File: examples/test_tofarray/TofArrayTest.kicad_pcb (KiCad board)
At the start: 2 copper layers, 30 x 55 mm, 44 parts, among them sw1 3.9x2.9mm Switch

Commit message: updated netlist
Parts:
- removed leds.led[5].package, leds.led[6].package, leds.led[7].package: KT-0603R (Hubei KENTO Elec) - Red 615~630nm 1.9~2.2V 0603 L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, LED_SMD:LED_0603_1608Metric
- removed leds.led[5].res, leds.led[6].res, leds.led[7].res: 0603WAF1001T5E (UNI-ROYAL(Uniroyal Elec)) - ±1% 1/10W Thick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, Resistor_SMD:R_0603_1608Metric
- removed the mcu.crystal.package at (128.1, -34.3)
- removed the mcu.swd at (88.0, -19.0)
- added i2c_pull.scl_res: 0603WAF4701T5E (UNI-ROYAL(Uniroyal Elec)) - ±1% 1/10W Thick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, Resistor_SMD:R_0603_1608Metric, F.Cu at (135.2, 48.9)
- added i2c_pull.sda_res: 0603WAF4701T5E (UNI-ROYAL(Uniroyal Elec)) - ±1% 1/10W Thick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, Resistor_SMD:R_0603_1608Metric, F.Cu at (131.2, 48.9)
- added mcu.crystal.package: X322512MSB4SI (Yangxing Tech) - 12MHz SMD Crystal Resonator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, Crystal_SMD_3225-4Pin_3.2x2.5mm, F.Cu at (211.1, 40.7)
- added mcu.swd: SWD, Connector:Tag-Connect_TC2050-IDC-FP_2x05_P1.27mm_Vertical, F.Cu at (170.0, 53.0)
- added rgb.blue_res: 0603WAF1001T5E (UNI-ROYAL(Uniroyal Elec)) - ±1% 1/10W Thick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, Resistor_SMD:R_0603_1608Metric, F.Cu at (132.1, 41.3)
- added rgb.green_res: 0603WAF1001T5E (UNI-ROYAL(Uniroyal Elec)) - ±1% 1/10W Thick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, Resistor_SMD:R_0603_1608Metric, F.Cu at (136.1, 38.8)
- added rgb.package: EAST1616RGBB2 (Everlight Electronics Co Ltd), LED_SMD:LED_LiteOn_LTST-C19HE1WT, F.Cu at (135.7, 41.9)
- added rgb.red_res: 0603WAF1001T5E (UNI-ROYAL(Uniroyal Elec)) - ±1% 1/10W Thick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, Resistor_SMD:R_0603_1608Metric, F.Cu at (132.1, 38.8)
- added spk: B2B-PH-K (JST), Connector_JST:JST_PH_B2B-PH-K_1x02_P2.00mm_Vertical, F.Cu at (117.5, 50.3)
- added spk_dac.c: CL10B473KB8NNNC (Samsung Electro-Mechanics) - 50V 47nF X7R 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, Capacitor_SMD:C_0603_1608Metric, F.Cu at (116.5, 58.4)
- added spk_dac.r: 0603WAF1001T5E (UNI-ROYAL(Uniroyal Elec)) - ±1% 1/10W Thick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, Resistor_SMD:R_0603_1608Metric, F.Cu at (120.5, 58.4)
- added spk_drv.bulk_cap: CL21A475KAQNNNE (Samsung Electro-Mechanics) - 25V 4.7uF X5R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, Capacitor_SMD:C_0805_2012Metric, F.Cu at (164.9, 46.9)
- added spk_drv.ic: TPA2005D1 (Texas Instruments), Package_SO:MSOP-8-1EP_3x3mm_P0.65mm_EP1.68x1.88mm_ThermalVias, F.Cu at (236.9, 50.3)
- added spk_drv.inn_cap: CL10A105KB8NNNC (Samsung Electro-Mechanics) - 50V 1uF X5R ±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, Capacitor_SMD:C_0603_1608Metric, F.Cu at (124.5, 38.8)
- added spk_drv.inn_res: 0603WAF3002T5E (UNI-ROYAL(Uniroyal Elec)) - ±1% 1/10W Thick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, Resistor_SMD:R_0603_1608Metric, F.Cu at (116.5, 38.8)
- added spk_drv.inp_cap: CL10A105KB8NNNC (Samsung Electro-Mechanics) - 50V 1uF X5R ±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, Capacitor_SMD:C_0603_1608Metric, F.Cu at (116.5, 41.3)
- added spk_drv.inp_res: 0603WAF3002T5E (UNI-ROYAL(Uniroyal Elec)) - ±1% 1/10W Thick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, Resistor_SMD:R_0603_1608Metric, F.Cu at (120.5, 38.8)
- added spk_drv.pwr_cap: CC0603KRX7R9BB104 (YAGEO) - 50V 100nF X7R ±10% 0603 Multila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, Capacitor_SMD:C_0603_1608Metric, F.Cu at (120.5, 41.3)
- added tof.elt[0].ic: VL53L0X (STMicroelectronics), OptoDevice:ST_VL53L0X, F.Cu at (155.5, 54.3)
- added tof.elt[0].vdd_cap[0]: CC0603KRX7R9BB104 (YAGEO) - 50V 100nF X7R ±10% 0603 Multila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, Capacitor_SMD:C_0603_1608Metric, F.Cu at (162.7, 38.8)
- added tof.elt[0].vdd_cap[1]: CL21A475KAQNNNE (Samsung Electro-Mechanics) - 25V 4.7uF X5R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, Capacitor_SMD:C_0805_2012Metric, F.Cu at (158.5, 39.0)
- added tof.elt[1].ic: VL53L0X (STMicroelectronics), OptoDevice:ST_VL53L0X, F.Cu at (170.8, 39.5)
- added tof.elt[1].vdd_cap[0]: CC0603KRX7R9BB104 (YAGEO) - 50V 100nF X7R ±10% 0603 Multila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, Capacitor_SMD:C_0603_1608Metric, F.Cu at (147.4, 48.2)
- added tof.elt[1].vdd_cap[1]: CL21A475KAQNNNE (Samsung Electro-Mechanics) - 25V 4.7uF X5R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, Capacitor_SMD:C_0805_2012Metric, F.Cu at (143.1, 48.5)
- added tof.elt[2].ic: VL53L0X (STMicroelectronics), OptoDevice:ST_VL53L0X, F.Cu at (240.0, 44.0)
- added tof.elt[2].vdd_cap[0]: CC0603KRX7R9BB104 (YAGEO) - 50V 100nF X7R ±10% 0603 Multila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, Capacitor_SMD:C_0603_1608Metric, F.Cu at (132.7, 58.4)
- added tof.elt[2].vdd_cap[1]: CL21A475KAQNNNE (Samsung Electro-Mechanics) - 25V 4.7uF X5R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, Capacitor_SMD:C_0805_2012Metric, F.Cu at (128.5, 58.7)
- added tof.elt[3].ic: VL53L0X (STMicroelectronics), OptoDevice:ST_VL53L0X, F.Cu at (155.5, 47.3)
- added tof.elt[3].vdd_cap[0]: CC0603KRX7R9BB104 (YAGEO) - 50V 100nF X7R ±10% 0603 Multila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, Capacitor_SMD:C_0603_1608Metric, F.Cu at (228.0, 49.4)
- added tof.elt[3].vdd_cap[1]: CL21A475KAQNNNE (Samsung Electro-Mechanics) - 25V 4.7uF X5R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, Capacitor_SMD:C_0805_2012Metric, F.Cu at (223.7, 49.6)
- added tof.elt[4].ic: VL53L0X (STMicroelectronics), OptoDevice:ST_VL53L0X, F.Cu at (140.9, 57.5)
- added tof.elt[4].vdd_cap[0]: CC0603KRX7R9BB104 (YAGEO) - 50V 100nF X7R ±10% 0603 Multila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, Capacitor_SMD:C_0603_1608Metric, F.Cu at (151.1, 38.8)
- added tof.elt[4].vdd_cap[1]: CL21A475KAQNNNE (Samsung Electro-Mechanics) - 25V 4.7uF X5R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, Capacitor_SMD:C_0805_2012Metric, F.Cu at (146.9, 39.0)
- mcu.crystal.cap_a, mcu.crystal.cap_b: value CL10C100JB8NNNC (Samsung Electro-Mechanics) - 50V 10pF C0G ±5% 0603 Multilayer Ceramic Capacitors MLCC - SMD/SMT ROHS -> CL10C330JB8NNNC (Samsung Electro-Mechanics) - 50V 33pF C0G ±5% 0603 Multilayer Ceramic Capacitors MLCC - SMD/SMT ROHS
- moved jlc_th3 135.0 mm to (248.0, 58.0)
- moved leds.led[0].res 117.0 mm to (237.0, 57.0)
- moved leds.led[1].package 111.9 mm to (199.3, 54.1)
- moved leds.led[2].package 111.9 mm to (210.7, 47.5)
- moved leds.led[2].res 111.9 mm to (229.8, 39.8)
- moved leds.led[3].res 111.9 mm to (214.8, 53.2)
- moved leds.led[4].package 111.9 mm to (222.1, 39.8)
- moved mcu.crystal.cap_a 111.9 mm to (187.5, 54.1)
- moved mcu.crystal.cap_b 111.9 mm to (191.5, 54.1)
- moved mcu.pwr_cap[0] 111.9 mm to (197.4, 40.0)
- moved mcu.pwr_cap[2] 111.9 mm to (197.2, 45.3)
- moved mcu.usb_pull 111.9 mm to (187.5, 48.2)
- moved mcu.vdda_cap_0 111.9 mm to (191.5, 48.2)
- moved mcu.vdda_cap_1 111.9 mm to (197.2, 42.8)
- moved mcu.pwr_cap[1] 111.9 mm to (201.2, 42.8)
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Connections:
- net leds.led[1].package.k renamed leds.led[1].res.a
- net leds.led[2].package.k renamed leds.led[2].res.a
- net leds.led[4].package.k renamed leds.led[4].res.a
- net mcu.gpio.leds_1 renamed leds_chain_0.1
- net usb.usb.dm renamed usb_chain_0.d_N
- net usb.usb.dp renamed usb_chain_0.d_P
- leds.led[0].package pad 2: mcu.gpio.leds_0 -> leds_chain_0.0
- leds.led[2].package pad 2: mcu.gpio.leds_2 -> leds_chain_0.2
- leds.led[3].package pad 2: mcu.gpio.leds_3 -> leds_chain_0.3
- leds.led[4].package pad 2: leds.signals.4 -> leds_chain_0.4
- mcu.ic pad 10: mcu.gpio.sw1 -> spk_chain_0
- mcu.ic pad 11: leds.signals.4 -> sw1_chain_0
- mcu.ic pad 12: leds.signals.5 -> tof.xshut.4
- mcu.ic pad 13: mcu.gpio.leds_0 -> mcu.gpio.tof_xshut_1
- mcu.ic pad 14: mcu.gpio.leds_2 -> tof.xshut.0
- mcu.ic pad 15: mcu.gpio.leds_7 -> mcu.gpio.tof_xshut_2
- mcu.ic pad 16: mcu.gpio.leds_3 -> tof.xshut.3
- mcu.ic pad 17: leds.signals.6 -> leds_chain_0.4
- mcu.ic pad 19: (no net) -> leds_chain_0.0
- mcu.ic pad 20: (no net) -> leds_chain_0.2
- mcu.ic pad 21: (no net) -> i2c_chain_0.scl
- mcu.ic pad 22: (no net) -> i2c_chain_0.sda
- mcu.ic pad 25: (no net) -> leds_chain_0.3
- mcu.ic pad 26: (no net) -> rgb_chain_0.red
- mcu.ic pad 27: (no net) -> rgb_chain_0.green
- mcu.ic pad 28: (no net) -> rgb_chain_0.blue
- mcu.ic pad 34: mcu.swd.swd.swdio -> mcu.ic.swd.swdio
- mcu.ic pad 39: mcu.swd.swd.swo -> mcu.ic.swd.swo
- mcu.ic pad 7: mcu.swd.swd.reset -> mcu.ic.swd.reset
- sw1 pad 2: mcu.gpio.sw1 -> sw1_chain_0
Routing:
- net gnd: track 56.3 -> 54.3 mm, vias 5 -> 2
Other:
- board size 30 x 55 mm -> 200 x 25 mm

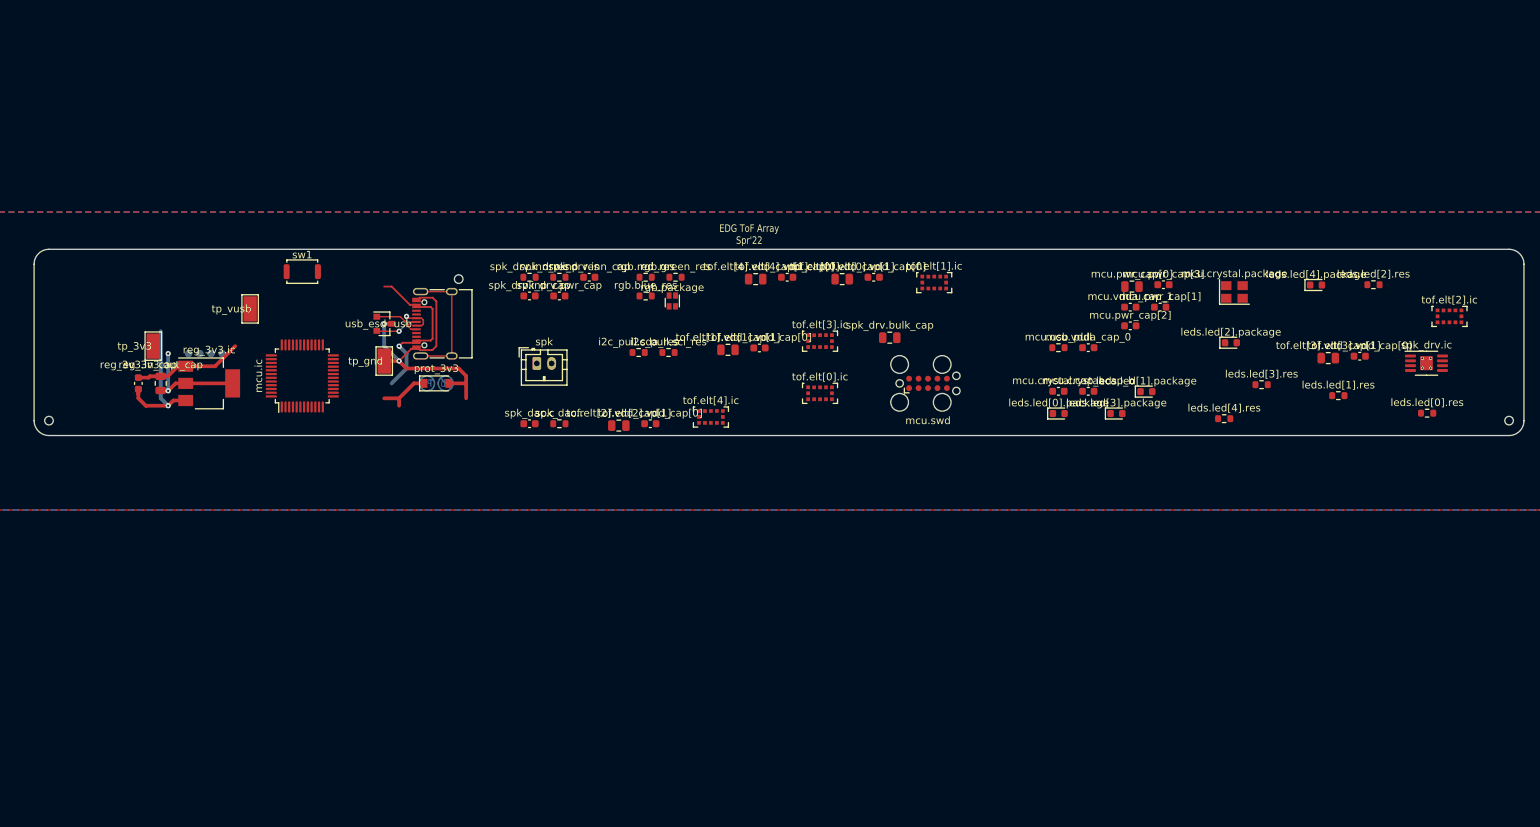
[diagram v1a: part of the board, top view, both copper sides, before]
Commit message: coarse placement of ToF array
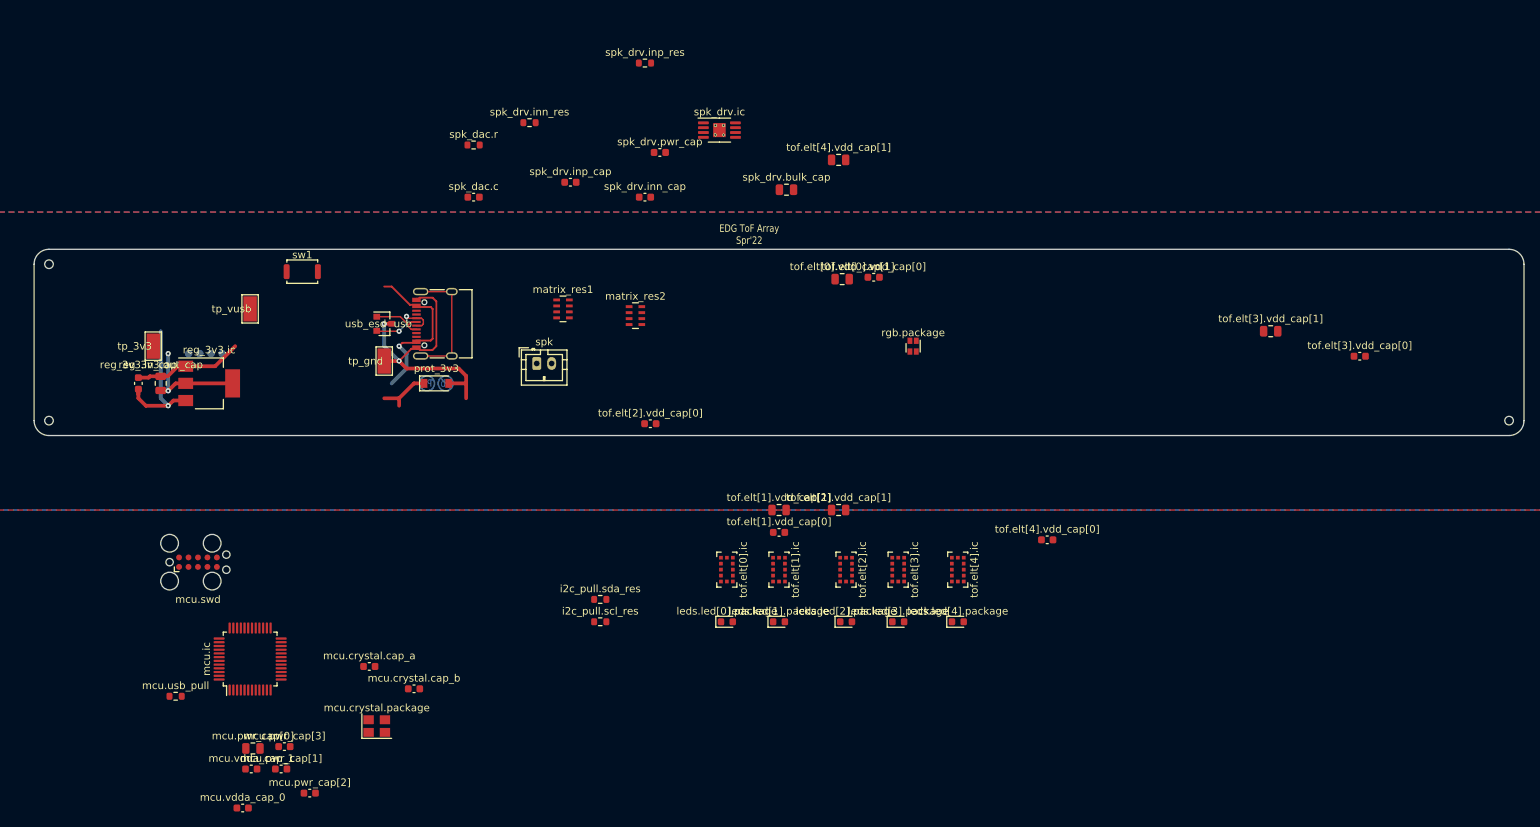
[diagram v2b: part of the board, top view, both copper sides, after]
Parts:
- removed leds.led[0].res, leds.led[1].res, leds.led[2].res, leds.led[3].res, leds.led[4].res, rgb.blue_res, rgb.green_res, rgb.red_res: 0603WAF1001T5E (UNI-ROYAL(Uniroyal Elec)) - ±1% 1/10W Thick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, Resistor_SMD:R_0603_1608Metric
- added matrix_res1: 4D03WGJ0102T5E (UNI-ROYAL(Uniroyal Elec)) - 4 ±5% 8 1kΩ 1/1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, Resistor_SMD:R_Array_Concave_4x0603, F.Cu at (121.0, 43.0)
- added matrix_res2: 4D03WGJ0102T5E (UNI-ROYAL(Uniroyal Elec)) - 4 ±5% 8 1kΩ 1/1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, Resistor_SMD:R_Array_Concave_4x0603, F.Cu at (130.7, 43.9)
- moved mcu.pwr_cap[0] 133.3 mm to (79.4, 102.0)
- moved mcu.vdda_cap_1 133.3 mm to (79.2, 104.8)
- moved mcu.pwr_cap[1] 133.3 mm to (83.2, 104.8)
- moved mcu.pwr_cap[3] 133.3 mm to (83.6, 101.8)
- moved mcu.vdda_cap_0 129.2 mm to (78.0, 110.0)
- moved mcu.crystal.package 129.0 mm to (96.0, 99.0)
- moved mcu.usb_pull 127.4 mm to (69.0, 95.0)
- moved mcu.pwr_cap[2] 126.8 mm to (87.0, 108.0)
- moved mcu.swd 100.9 mm to (72.0, 77.0)
- moved spk_drv.ic 99.9 mm to (142.0, 19.0)
- moved mcu.crystal.cap_a 99.6 mm to (95.0, 91.0)
- moved mcu.crystal.cap_b 98.9 mm to (101.0, 94.0)
- moved tof.elt[2].ic 87.8 mm to (159.0, 78.0), turned to 270 degrees
- moved leds.led[4].package 66.0 mm to (174.0, 85.0)
- moved leds.led[2].package 63.8 mm to (159.0, 85.0)
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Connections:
- net mcu.crystal.crystal.b renamed mcu.ic.osc.xtal_out
- net mcu.gpio.tof_xshut_1 renamed tof.xshut.1
- net mcu.gpio.tof_xshut_2 renamed tof.xshut.2
- net mcu.ic.swd.reset renamed mcu.swd.swd.reset
- net mcu.ic.swd.swclk renamed mcu.swd.swd.swclk
- net tof.xshut.0 renamed mcu.gpio.tof_xshut_0
- net tof.xshut.4 renamed mcu.gpio.tof_xshut_4
- net usb.shield renamed usb.S1
- leds.led[0].package pad 1: leds.led[0].res.a -> matrix_res1.a.0
- leds.led[1].package pad 1: leds.led[1].res.a -> matrix_res1.a.1
- leds.led[2].package pad 1: leds.led[2].res.a -> matrix_res1.a.2
- leds.led[3].package pad 1: leds.led[3].package.k -> matrix_res1.a.3
- leds.led[4].package pad 1: leds.led[4].res.a -> matrix_res2.a.0
- mcu.ic pad 26: rgb_chain_0.red -> rgb_chain_0.green
- mcu.ic pad 27: rgb_chain_0.green -> rgb_chain_0.blue
- mcu.ic pad 28: rgb_chain_0.blue -> rgb_chain_0.red
- rgb.package pad 1: rgb.package.k_blue -> matrix_res2.a.3
- rgb.package pad 3: rgb.red_res.a -> matrix_res2.a.1
- rgb.package pad 4: rgb.package.k_green -> matrix_res2.a.2

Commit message: continued coarse placement
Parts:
- moved tof.elt[3].vdd_cap[0] 66.3 mm to (166.0, 73.0)
- moved tof.elt[3].vdd_cap[1] 55.5 mm to (166.0, 70.0)
- moved tof.elt[4].vdd_cap[1] 49.6 mm to (174.0, 70.0)
- moved tof.elt[0].vdd_cap[0] 39.5 mm to (143.0, 73.0)
- moved tof.elt[0].vdd_cap[1] 34.6 mm to (143.0, 70.0)
- moved mcu.crystal.package 30.5 mm to (68.0, 87.0), turned to 90 degrees
- moved mcu.crystal.cap_b 30.1 mm to (72.0, 86.0)
- moved tof.elt[2].vdd_cap[0] 30.1 mm to (159.0, 73.0)
- moved spk_drv.bulk_cap 24.2 mm to (129.0, 17.0)
- moved mcu.crystal.cap_a 23.2 mm to (72.0, 88.0)
- moved mcu.pwr_cap[3] 21.1 mm to (80.0, 81.0), turned to 180 degrees
- moved mcu.swd 20.1 mm to (52.0, 75.0)
- moved mcu.vdda_cap_0 18.4 mm to (71.0, 93.0), turned to 90 degrees
- moved mcu.pwr_cap[2] 18.1 mm to (89.0, 90.0), turned to 270 degrees
- moved mcu.pwr_cap[0] 16.7 mm to (91.0, 90.0), turned to 270 degrees
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
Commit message: coarse placement 2
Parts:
- moved matrix_res1 81.9 mm to (193.0, 4.00)
- moved matrix_res2 81.9 mm to (202.7, 4.91)
- moved tp_gnd 81.9 mm to (169.0, 11.0)
- moved leds.led[0].package 78.2 mm to (70.0, 57.0)
- moved tof.elt[0].ic 78.2 mm to (70.0, 50.0)
- moved tof.elt[0].vdd_cap[0] 78.2 mm to (70.0, 45.0)
- moved tof.elt[0].vdd_cap[1] 78.2 mm to (70.0, 42.0)
- moved mcu.pwr_cap[1] 74.2 mm to (139.0, 54.0), turned to 0 degrees
- moved mcu.pwr_cap[2] 66.6 mm to (139.0, 46.0), turned to 0 degrees
- moved mcu.ic 64.0 mm to (130.0, 50.0)
- moved mcu.vdda_cap_1 63.8 mm to (121.0, 56.0), turned to 180 degrees
- moved mcu.vdda_cap_0 63.4 mm to (121.0, 54.0), turned to 180 degrees
- moved mcu.crystal.cap_a 62.8 mm to (122.0, 50.0), turned to 270 degrees
- moved leds.led[4].package 62.6 mm to (230.0, 57.0)
- moved tof.elt[4].ic 62.6 mm to (230.0, 50.0)
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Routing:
- net v3v3: track 22.2 -> 63.6 mm, vias 2 -> 6
- net vusb: track 42.7 -> 19.4 mm, vias 2 -> 1
- net gnd: track 54.3 -> 32.6 mm, vias 2 -> 11
- net usb.S1: track 17.0 -> 0.00 mm
- net mcu.crystal.crystal.a: track 0.00 -> 10.6 mm
- net usb_chain_0.d_P: track 9.43 -> 0.00 mm, vias 2 -> 0
- net mcu.ic.osc.xtal_out: track 0.00 -> 8.55 mm
- net usb_chain_0.d_N: track 7.41 -> 0.00 mm

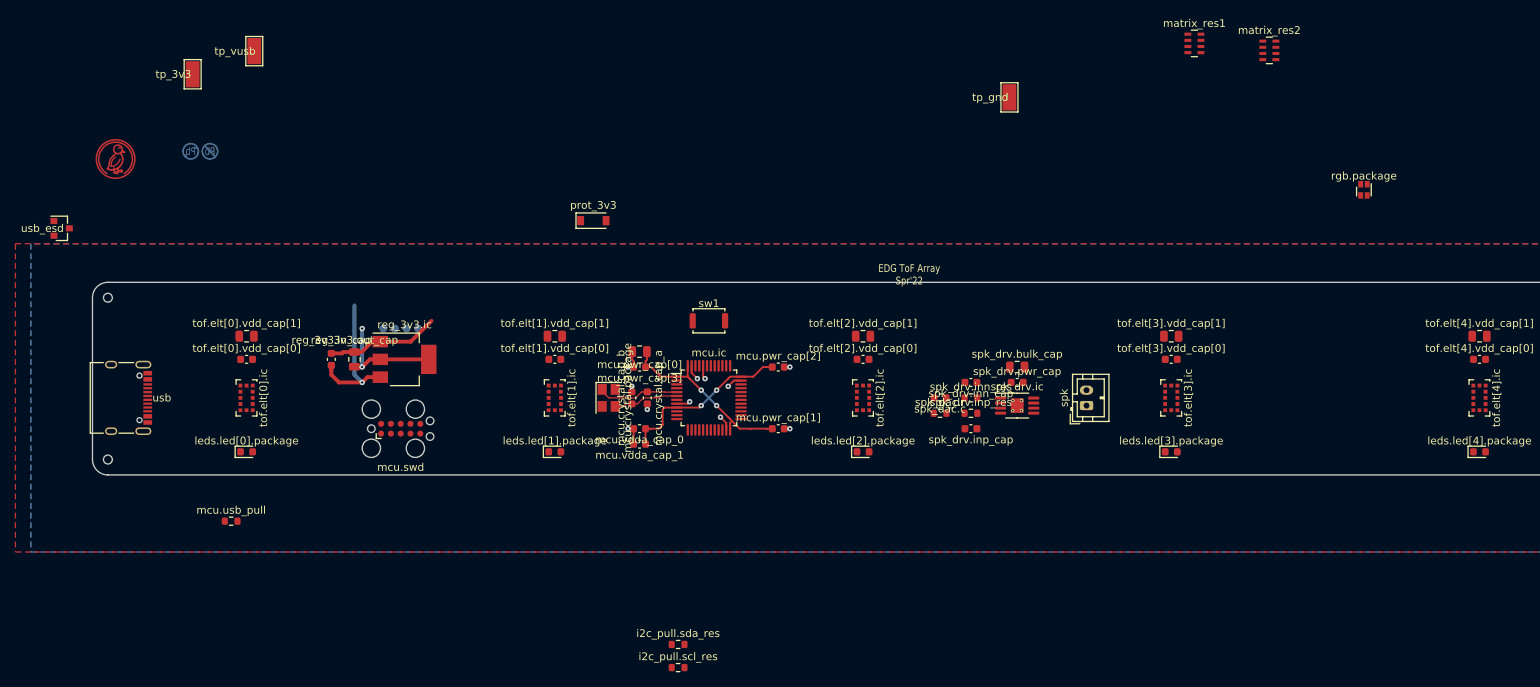
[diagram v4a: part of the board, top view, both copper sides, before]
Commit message: board layout wip, most subblocks routed
4 layers would make this so much easier
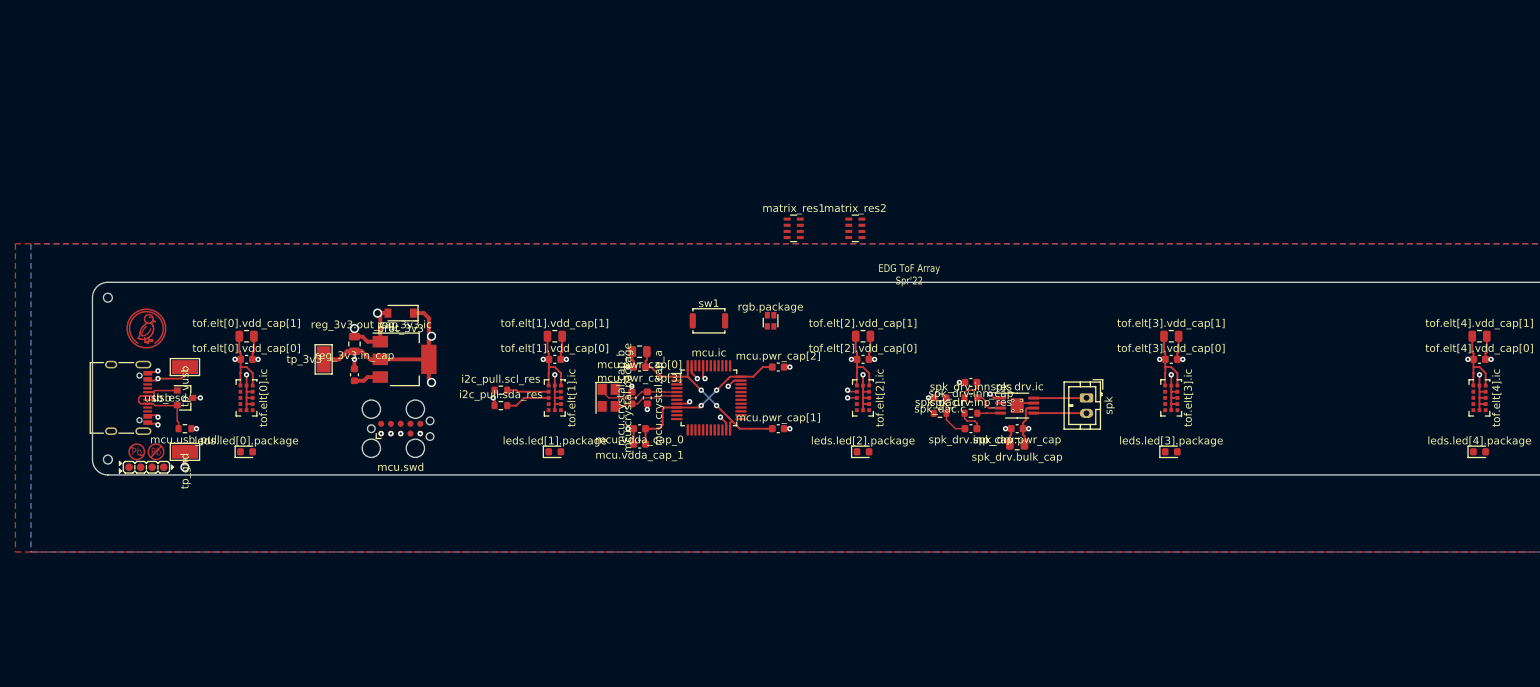
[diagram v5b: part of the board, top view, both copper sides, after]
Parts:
- id, leadfree: moved to F.Cu
- moved tp_gnd 116.5 mm to (62.0, 57.0), turned to 180 degrees
- moved rgb.package 78.9 mm to (138.0, 40.0)
- moved matrix_res2 58.5 mm to (149.0, 28.0)
- moved matrix_res1 57.3 mm to (141.0, 28.0)
- moved i2c_pull.scl_res 42.7 mm to (103.0, 49.0)
- moved tp_vusb 42.0 mm to (62.0, 46.0), turned to 180 degrees
- moved tp_3v3 40.7 mm to (80.0, 45.0)
- moved leadfree 39.6 mm to (57.0, 57.0)
- moved i2c_pull.sda_res 38.6 mm to (103.0, 51.0)
- moved id 37.6 mm to (57.0, 59.0)
- moved prot_3v3 27.7 mm to (90.0, 39.0), turned to 180 degrees
- moved usb_esd 27.2 mm to (62.0, 50.0)
- moved duck 22.4 mm to (57.0, 41.0)
- moved mcu.usb_pull 13.4 mm to (62.0, 54.0), turned to 180 degrees
- moved spk_drv.bulk_cap 10.0 mm to (170.0, 56.0), turned to 180 degrees
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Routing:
- net v3v3: track 63.6 -> 134.3 mm, vias 6 -> 14
- net gnd: track 32.6 -> 96.6 mm, vias 11 -> 34
- net usb_chain_0.d_P: track 0.00 -> 10.1 mm
- net i2c_chain_0.sda: track 0.00 -> 6.99 mm, vias 0 -> 1
- net spk_chain_2.b: track 0.00 -> 6.86 mm
- net spk_chain_2.a: track 0.00 -> 6.86 mm
- net i2c_chain_0.scl: track 0.00 -> 6.74 mm, vias 0 -> 1
- net spk_chain_1: track 0.00 -> 5.73 mm
- net usb_chain_0.d_N: track 0.00 -> 5.72 mm
- net spk_drv.(adapter)inn_res.b.src: track 0.00 -> 3.87 mm
- net spk_drv.inp_cap.pos: track 0.00 -> 3.25 mm
- net spk_drv.inn_cap.pos: track 0.00 -> 3.25 mm
- net spk_drv.(adapter)inp_res.b.src: track 0.00 -> 3.04 mm
- net vusb: track 19.4 -> 19.8 mm, vias 1 -> 4

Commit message: Update TofArrayTest.kicad_pcb
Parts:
- moved mcu.crystal.package 26.0 mm to (143.0, 50.0), turned to 90 degrees
- moved mcu.pwr_cap[0] 21.6 mm to (139.0, 56.0), turned to 0 degrees
- moved mcu.vdda_cap_1 21.6 mm to (139.0, 44.0), turned to 0 degrees
- moved mcu.crystal.cap_b 20.0 mm to (140.0, 50.0), turned to 270 degrees
- moved mcu.pwr_cap[1] 19.7 mm to (121.0, 46.0), turned to 180 degrees
- moved mcu.pwr_cap[2] 19.7 mm to (121.0, 54.0), turned to 180 degrees
- moved mcu.pwr_cap[3] 19.7 mm to (139.0, 54.0), turned to 0 degrees
- moved mcu.vdda_cap_0 19.7 mm to (139.0, 46.0), turned to 0 degrees
- moved rgb.package 17.9 mm to (130.0, 24.0)
- moved sw1 17.2 mm to (120.0, 26.0)
- moved mcu.crystal.cap_a 16.0 mm to (138.0, 50.0), turned to 90 degrees
- moved prot_3v3 10.0 mm to (98.0, 45.0), turned to 270 degrees
- moved tof.elt[0].vdd_cap[1] 1.00 mm to (70.0, 43.0)
- moved tof.elt[1].vdd_cap[1] 1.00 mm to (110.0, 43.0)
- moved tof.elt[2].vdd_cap[1] 1.00 mm to (150.0, 43.0)
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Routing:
- net i2c_chain_0.sda: track 6.99 -> 225.1 mm, vias 1 -> 10
- net i2c_chain_0.scl: track 6.74 -> 213.5 mm, vias 1 -> 10
- net gnd: track 96.6 -> 87.0 mm
- net v3v3: track 134.3 -> 126.7 mm
